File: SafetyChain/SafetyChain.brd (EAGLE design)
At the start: 74.6 x 52.1 mm, 33 parts, among them T1_SMT BTA16, T1_THT BTA16

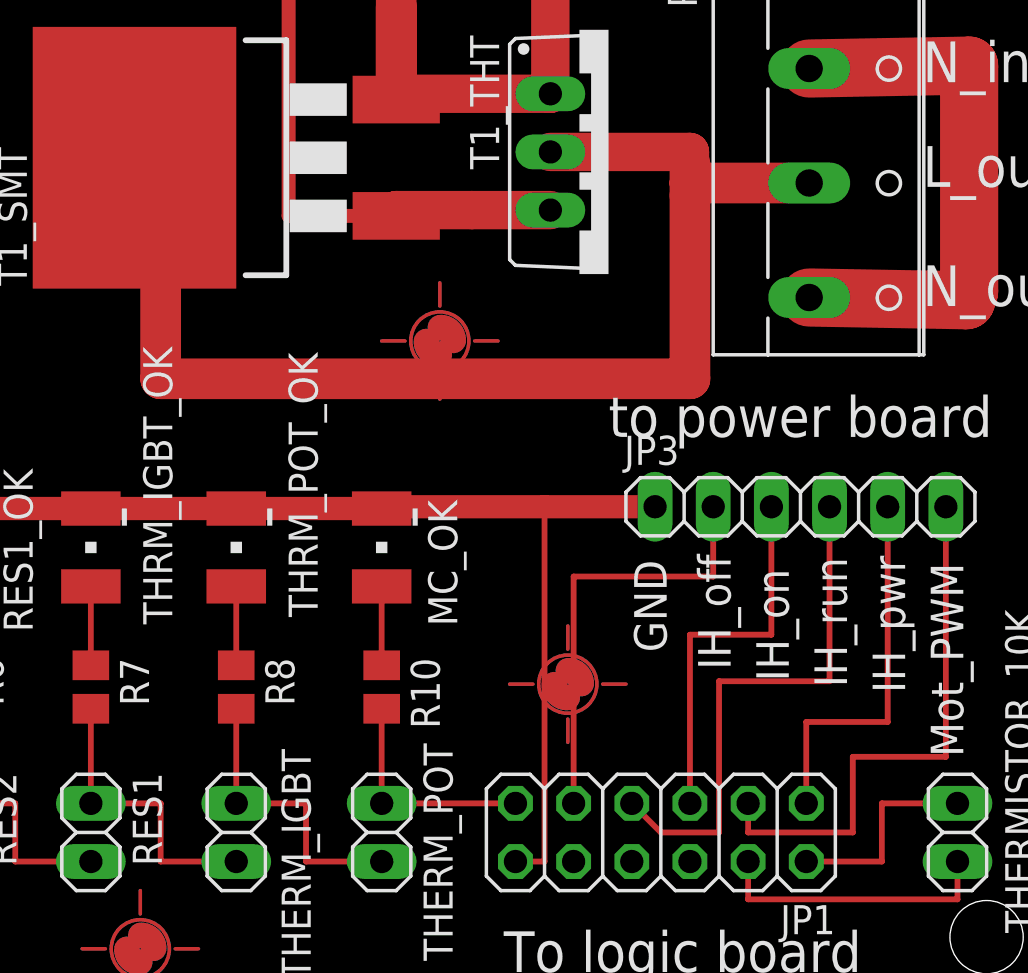
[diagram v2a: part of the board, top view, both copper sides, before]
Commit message: Changed USB connectors, created gerber Files
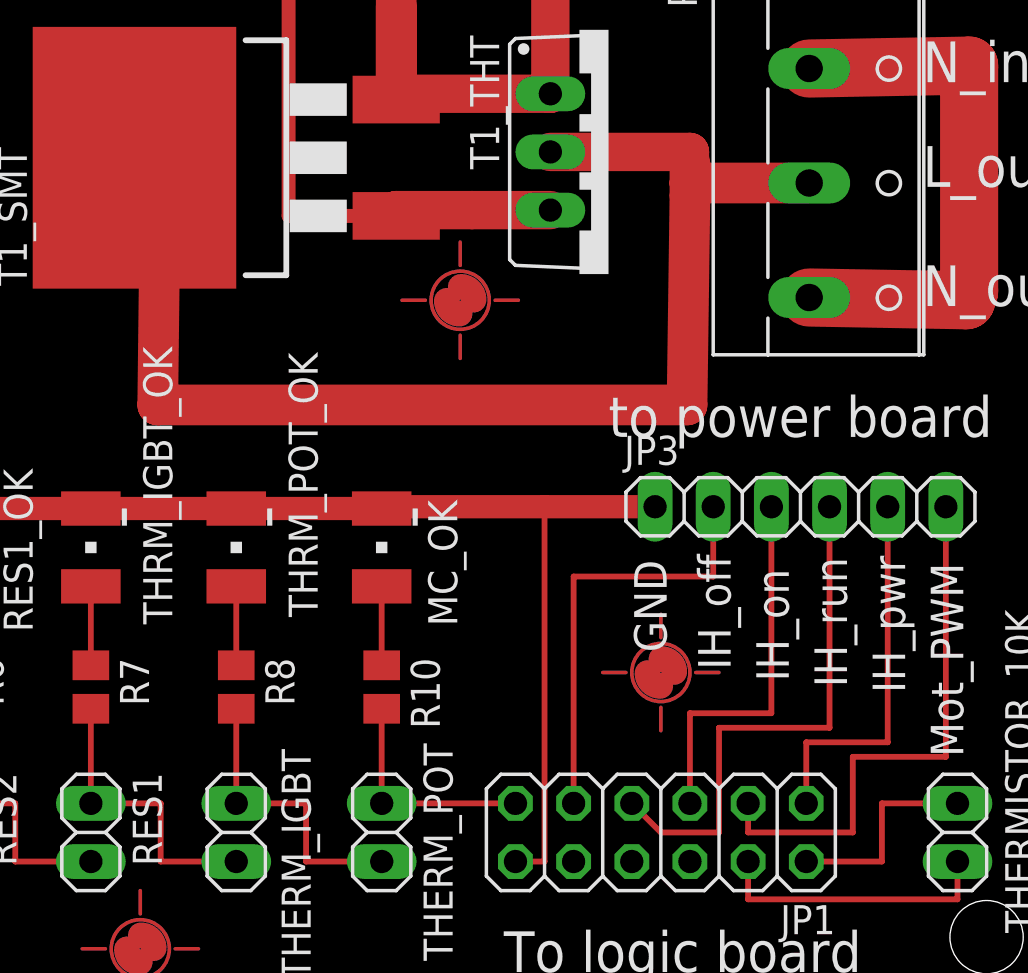
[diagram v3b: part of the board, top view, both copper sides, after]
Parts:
- moved U$3 4.10 mm to (59.4, 15.4)
- moved U$2 1.99 mm to (50.7, 31.6)
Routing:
- net L_OUT: track 55.1 -> 57.4 mm
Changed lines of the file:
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@@
 <element name="T1_SMT" library="transistor-power" package="D2PACK" value="BTA16" x="38.989" y="37.846" rot="R90"/>
 <element name="U$1" library="marks" package="PASS-ROUND" value="" x="12.954" y="44.069"/>
-<element name="U$2" library="marks" package="PASS-ROUND" value="" x="49.784" y="29.845"/>
-<element name="U$3" library="marks" package="PASS-ROUND" value="" x="55.372" y="14.859"/>
+<element name="U$2" library="marks" package="PASS-ROUND" value="" x="50.673" y="31.623"/>
+<element name="U$3" library="marks" package="PASS-ROUND" value="" x="59.436" y="15.367"/>
 <element name="U$4" library="marks" package="PASS-ROUND" value="" x="36.703" y="3.302"/>
 <element name="T1_THT" library="triac" package="TO220BV" value="BTA16" x="57.15" y="38.1" rot="R270"/>
@@
 <wire x1="60.706" y1="36.743" x2="60.706" y2="37.592" width="1.778" layer="1"/>
 <wire x1="36.449" y1="37.846" x2="37.592" y2="37.846" width="1.778" layer="1"/>
-<wire x1="37.592" y1="37.846" x2="37.592" y2="28.194" width="1.778" layer="1"/>
-<wire x1="37.592" y1="28.194" x2="60.706" y2="28.194" width="1.778" layer="1"/>
-<wire x1="60.706" y1="28.194" x2="60.706" y2="36.195" width="1.778" layer="1"/>
+<wire x1="37.592" y1="37.846" x2="37.465" y2="27.051" width="1.778" layer="1"/>
+<wire x1="37.465" y1="27.051" x2="60.579" y2="27.051" width="1.778" layer="1"/>
+<wire x1="60.579" y1="27.051" x2="60.706" y2="36.195" width="1.778" layer="1"/>
 <contactref element="T1_THT" pad="T2"/>
 <wire x1="60.706" y1="36.195" x2="60.706" y2="36.743" width="1.778" layer="1"/>
@@
 <contactref element="JP3" pad="3"/>
 <contactref element="JP1" pad="5"/>
-<wire x1="64.262" y1="22.606" x2="64.262" y2="17.018" width="0.254" layer="1"/>
-<wire x1="64.262" y1="17.018" x2="60.706" y2="17.018" width="0.254" layer="1"/>
-<wire x1="60.706" y1="17.018" x2="60.706" y2="9.652" width="0.254" layer="1"/>
+<wire x1="64.262" y1="22.606" x2="64.262" y2="13.589" width="0.254" layer="1"/>
+<wire x1="64.262" y1="13.589" x2="60.706" y2="13.589" width="0.254" layer="1"/>
+<wire x1="60.706" y1="13.589" x2="60.706" y2="9.652" width="0.254" layer="1"/>
 </signal>
 <signal name="IH_RUN">
@@
 <wire x1="58.166" y1="9.652" x2="59.436" y2="8.382" width="0.254" layer="1"/>
 <wire x1="59.436" y1="8.382" x2="61.976" y2="8.382" width="0.254" layer="1"/>
-<wire x1="61.976" y1="8.382" x2="61.976" y2="14.986" width="0.254" layer="1"/>
-<wire x1="61.976" y1="14.986" x2="66.802" y2="14.986" width="0.254" layer="1"/>
-<wire x1="66.802" y1="14.986" x2="66.802" y2="22.606" width="0.254" layer="1"/>
+<wire x1="61.976" y1="8.382" x2="61.976" y2="12.954" width="0.254" layer="1"/>
+<wire x1="61.976" y1="12.954" x2="66.802" y2="12.954" width="0.254" layer="1"/>
+<wire x1="66.802" y1="12.954" x2="66.802" y2="22.606" width="0.254" layer="1"/>
 </signal>
 <signal name="IH_PWR">
 <contactref element="JP3" pad="5"/>
 <contactref element="JP1" pad="1"/>
-<wire x1="65.786" y1="9.652" x2="65.786" y2="13.208" width="0.254" layer="1"/>
-<wire x1="65.786" y1="13.208" x2="69.342" y2="13.208" width="0.254" layer="1"/>
-<wire x1="69.342" y1="13.208" x2="69.342" y2="22.606" width="0.254" layer="1"/>
+<wire x1="65.786" y1="9.652" x2="65.786" y2="12.319" width="0.254" layer="1"/>
+<wire x1="65.786" y1="12.319" x2="69.342" y2="12.319" width="0.254" layer="1"/>
+<wire x1="69.342" y1="12.319" x2="69.342" y2="22.606" width="0.254" layer="1"/>
 </signal>
 <signal name="MOT_PWM">

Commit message: Redesign of all boards.
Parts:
- removed T1_SMT: BTA16, transistor-power:D2PACK
- added PWR_SW_LED: (no value), pinhead:1X02
- R10, R4, R5, R6, R7, R8, R9: value 819 -> 1k
- moved U$3 0.76 mm to (59.4, 16.1)
- moved THERMISTOR_10K 0.51 mm to (72.4, 8.89)
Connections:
- net GND: now also PWR_SW_LED.2
- net L_IN: no longer T1_SMT.3
- net L_OUT: no longer T1_SMT.2
- net N$8: now also PWR_SW_LED.1
- net TRIAC_DRV: no longer T1_SMT.1
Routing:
- net L_OUT: track 57.4 -> 17.5 mm
- net GND: track 77.1 -> 92.0 mm
- net L_IN: track 67.0 -> 58.7 mm
- net N$8: track 50.9 -> 57.1 mm
- net TRIAC_DRV: track 59.9 -> 57.0 mm
- net PWR_N: track 24.1 -> 21.5 mm
- net IH_THERMISTOR: track 9.14 -> 9.65 mm
